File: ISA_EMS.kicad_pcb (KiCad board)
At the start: 2 copper layers, 176.5 x 85.1 mm, 49 parts, among them J1 ISA BUS, J2 EMS Address, U10 74HCT32, U11 74HCT04, U12 74LS245, U13 AS6C4008-55PCN, U14 AS6C4008-55PCN, U15 AS6C4008-55PCN, U16 AS6C4008-55PCN, U17 74HCT138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

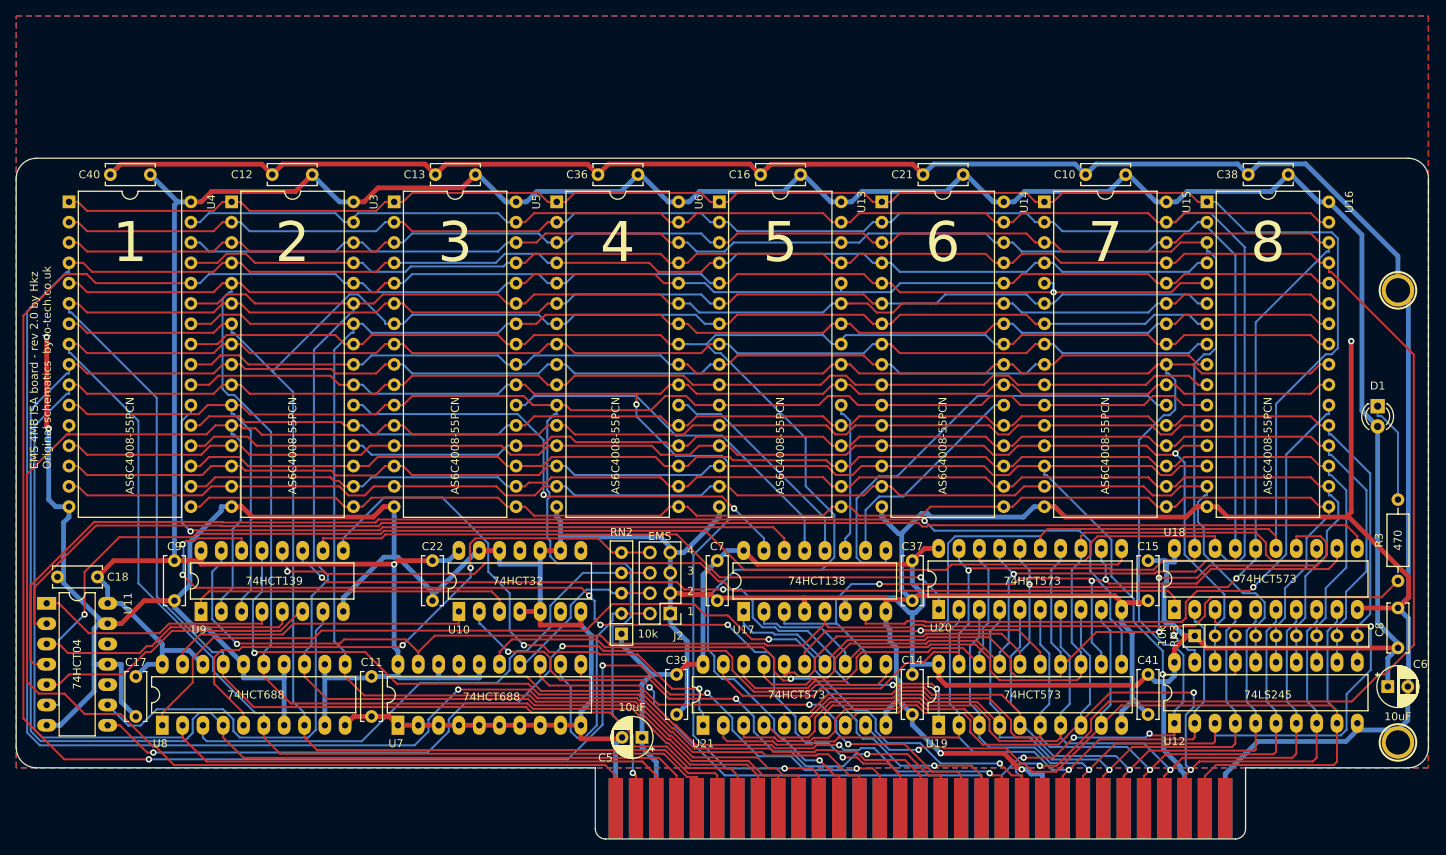
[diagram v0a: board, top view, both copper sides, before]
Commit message: Replace components on board
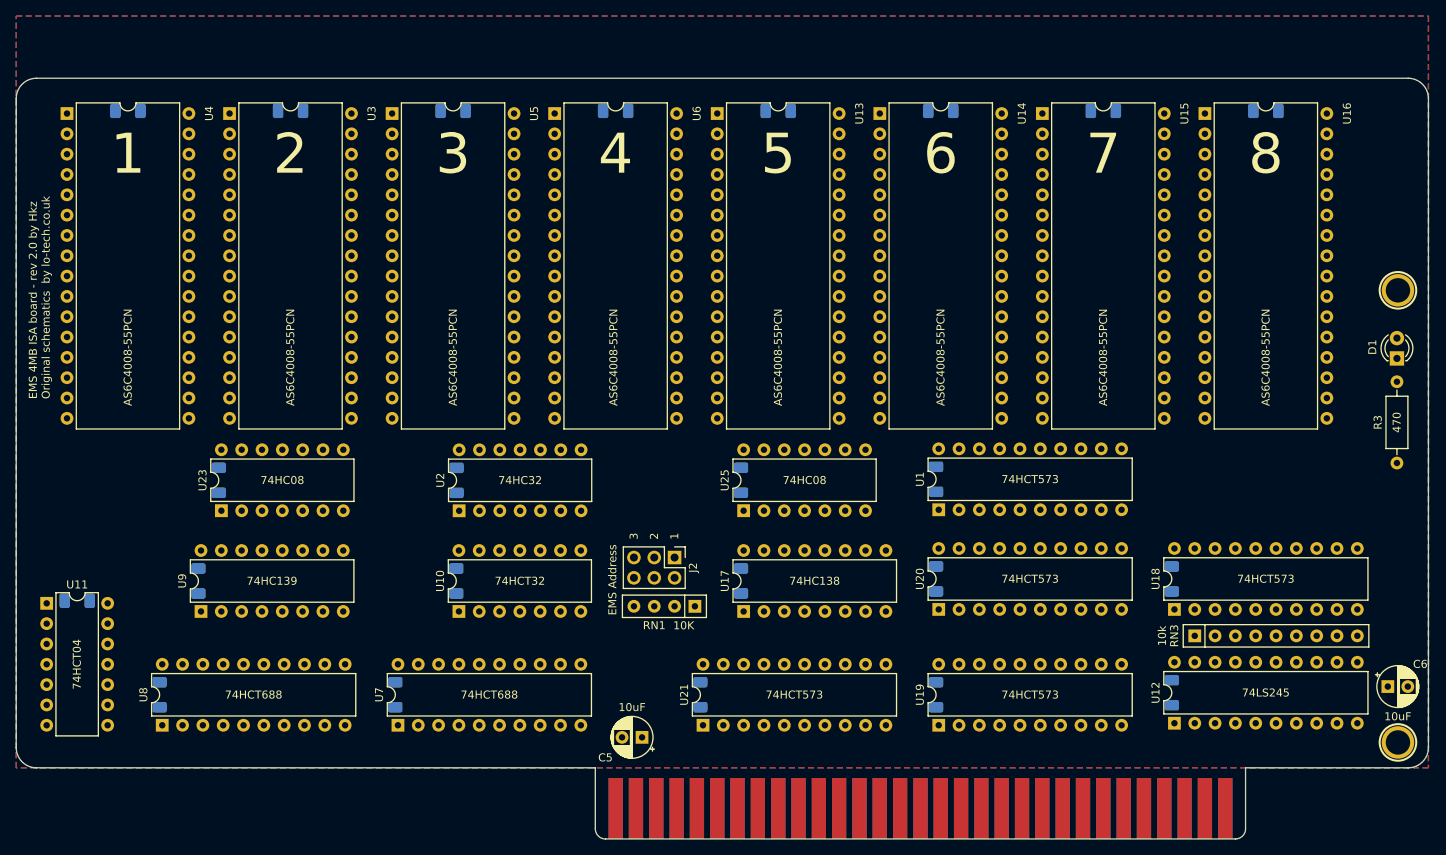
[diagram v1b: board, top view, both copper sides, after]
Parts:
- removed RN2: 10k, Resistor_THT:R_Array_SIP5
- added C1: 100nF, Capacitor_SMD:C_1206_3216Metric_Pad1.33x1.80mm_HandSolder, B.Cu at (193.5, 158.4)
- added C2: 100nF, Capacitor_SMD:C_1206_3216Metric_Pad1.33x1.80mm_HandSolder, B.Cu at (163.7, 158.4)
- added C3: 100nF, Capacitor_SMD:C_1206_3216Metric_Pad1.33x1.80mm_HandSolder, B.Cu at (253.4, 158.2)
- added RN1: 10K, Resistor_THT:R_Array_SIP4, F.Cu at (223.3, 174.1)
- added U1: 74HCT573, Package_DIP:DIP-20_W7.62mm, F.Cu at (253.7, 162.1)
- added U2: 74HC32, Package_DIP:DIP-14_W7.62mm, F.Cu at (193.8, 162.2)
- added U23: 74HC08, Package_DIP:DIP-14_W7.62mm, F.Cu at (164.1, 162.2)
- added U25: 74HC08, Package_DIP:DIP-14_W7.62mm, F.Cu at (229.4, 162.2)
- C10, C11, C12, C13, C14, C15, C16, C17, C18, C21, C22, C36, C37, C38, C39, C40, C41, C7, C8, C9: footprint Capacitor_THT:C_Disc_D6.0mm_W2.5mm_P5.00mm -> Capacitor_SMD:C_1206_3216Metric_Pad1.33x1.80mm_HandSolder; moved to B.Cu
- J2: footprint Connector_PinHeader_2.54mm:PinHeader_2x04_P2.54mm_Vertical -> Connector_PinHeader_2.54mm:PinHeader_2x03_P2.54mm_Vertical
- U10, U11: footprint Package_DIP:DIP-14_W7.62mm_LongPads -> Package_DIP:DIP-14_W7.62mm
- U12, U18, U19, U20, U21, U7, U8: footprint Package_DIP:DIP-20_W7.62mm_LongPads -> Package_DIP:DIP-20_W7.62mm
- U17: value 74HCT138 -> 74HC138; footprint Package_DIP:DIP-16_W7.62mm_LongPads -> Package_DIP:DIP-16_W7.62mm
- U9: value 74HCT139 -> 74HC139; footprint Package_DIP:DIP-16_W7.62mm_LongPads -> Package_DIP:DIP-16_W7.62mm
- moved C8 84.8 mm to (229.0, 158.4), turned to -90 degrees
- moved R3 14.7 mm to (311.0, 156.2)
- moved U13 11.0 mm to (226.1, 112.5)
- moved U14 11.0 mm to (246.4, 112.5)
- moved U15 11.0 mm to (266.7, 112.5)
- moved U16 11.0 mm to (287.0, 112.5)
- moved U3 11.0 mm to (165.1, 112.5)
- moved U4 11.0 mm to (144.8, 112.5)
- moved U5 11.0 mm to (185.4, 112.5)
- moved U6 11.0 mm to (205.7, 112.5)
- moved C38 8.44 mm to (294.6, 112.2)
- moved C13 8.44 mm to (193.0, 112.2)
- moved C10 8.44 mm to (274.3, 112.2)
- moved C16 8.44 mm to (233.7, 112.2)
- moved C21 8.44 mm to (254.0, 112.2)
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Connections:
- net /~IOW renamed /~{IOW}
- net /~MEMR renamed /~{MEMR}
- net /~MEMW renamed /~{MEMW}
- net /~RAM-CS0 renamed /~{RAM-CS0}
- net /~RAM-CS1 renamed /~{RAM-CS1}
- net /~RAM-CS2 renamed /~{RAM-CS2}
- net /~RAM-CS3 renamed /~{RAM-CS3}
- net /~RAM-CS4 renamed /~{RAM-CS4}
- net /~RAM-CS5 renamed /~{RAM-CS5}
- net /~RAM-CS6 renamed /~{RAM-CS6}
- net /~RAM-CS7 renamed /~{RAM-CS7}
- net /~RAM-SELECT renamed /~{RAM-SELECT}
- net /~REG0-OE renamed /~{REG0-OE}
- net /~REG1-OE renamed /~{REG1-OE}
- net /~REG2-OE renamed /~{REG2-OE}
- net /~REG3-OE renamed /~{REG3-OE}
- J1 pad 14: (no net) -> /~{IOR}
- J1 pad 15: (no net) -> unconnected-(J1-~{DACK3}-Pad15)
- J1 pad 16: (no net) -> unconnected-(J1-DRQ3-Pad16)
- J1 pad 17: (no net) -> unconnected-(J1-~{DACK1}-Pad17)
- J1 pad 18: (no net) -> unconnected-(J1-DRQ1-Pad18)
- J1 pad 19: (no net) -> unconnected-(J1-~{DACK0}-Pad19)
- J1 pad 2: (no net) -> /RESETDRV
- J1 pad 20: (no net) -> unconnected-(J1-CLK-Pad20)
- J1 pad 21: (no net) -> /IRQ7
- J1 pad 22: (no net) -> /IRQ6
- J1 pad 23: (no net) -> /IRQ5
- J1 pad 24: (no net) -> /IRQ4
- J1 pad 25: (no net) -> /IRQ3
- J1 pad 26: (no net) -> /~{DACK2}
- J1 pad 27: (no net) -> /TC
- J1 pad 28: (no net) -> unconnected-(J1-ALE-Pad28)
- J1 pad 30: (no net) -> unconnected-(J1-OSC-Pad30)
- J1 pad 32: (no net) -> unconnected-(J1-IO-Pad32)
- J1 pad 4: (no net) -> unconnected-(J1-IRQ2-Pad4)
- J1 pad 41: (no net) -> unconnected-(J1-IO_READY-Pad41)
- J1 pad 5: (no net) -> unconnected-(J1--5V-Pad5)
- J1 pad 6: (no net) -> /DRQ2
- J1 pad 7: (no net) -> -12V
- J1 pad 8: (no net) -> unconnected-(J1-UNUSED-Pad8)
- J1 pad 9: (no net) -> +12V
- U10 pad 10: GND -> Net-(U10-Pad10)
- U10 pad 11: (no net) -> unconnected-(U10-Pad11)
- U10 pad 4: GND -> Net-(U10-Pad3)
- U10 pad 5: GND -> /A2
- U10 pad 6: (no net) -> Net-(U9A-E)
- U10 pad 8: (no net) -> Net-(U10-Pad8)
- U10 pad 9: GND -> Net-(U10-Pad3)
- U11 pad 10: (no net) -> Net-(U10-Pad10)
- U11 pad 11: GND -> /A2
- U11 pad 12: (no net) -> Net-(U1-Load)
- U11 pad 13: GND -> Net-(U10-Pad8)
- U17 pad 4: GND -> /RAM-DISABLED
- U8 pad 2: /A2 -> GND
- U8 pad 3: /JP3 -> GND
- U8 pad 5: /JP4 -> /JP3
- U9 pad 1: Net-(U10-Pad3) -> Net-(U9A-E)
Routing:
- net GND: track 825.8 -> 0.00 mm, vias 5 -> 0
- net VCC: track 600.8 -> 0.00 mm, vias 1 -> 0
- net /A13: track 352.3 -> 0.00 mm, vias 4 -> 0
- net /A12: track 327.0 -> 0.00 mm, vias 1 -> 0
- net /RAM-A18: track 304.4 -> 0.00 mm, vias 1 -> 0
- net /A0: track 290.2 -> 0.00 mm
- net /RAM-A15: track 290.0 -> 0.00 mm
- net /A3: track 288.7 -> 0.00 mm
- net /A2: track 281.1 -> 0.00 mm
- net /A6: track 278.6 -> 0.00 mm
- net /RAM-A17: track 274.7 -> 0.00 mm, vias 2 -> 0
- net /A7: track 274.2 -> 0.00 mm, vias 1 -> 0
- net /RAM-A16: track 273.0 -> 0.00 mm, vias 1 -> 0
- net /RAM-A14: track 270.9 -> 0.00 mm, vias 1 -> 0
- net /A4: track 268.9 -> 0.00 mm
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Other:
- board size 176.5 x 85.1 mm -> 176.5 x 95.1 mm
- net class Default removed
- net class POWER removed
- net class POWR_SMALL removed
- board text added: "260-267h"
- board text added: "268-26Fh"
- board text removed: "260-263h"
- board text removed: "264-267h"
- board text removed: "268-26Bh"
- board text removed: "26C-26Fh"
- board text removed: "EMS"

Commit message: Begin routing
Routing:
- net /D7: track 0.00 -> 97.6 mm, vias 0 -> 2
- net /D6: track 0.00 -> 96.2 mm, vias 0 -> 2
- net VCC: track 0.00 -> 95.9 mm
- net /D5: track 0.00 -> 95.6 mm, vias 0 -> 2
- net /D4: track 0.00 -> 94.5 mm, vias 0 -> 2
- net /D3: track 0.00 -> 93.3 mm, vias 0 -> 2
- net /D2: track 0.00 -> 92.3 mm, vias 0 -> 2
- net /D1: track 0.00 -> 90.8 mm, vias 0 -> 2
- net /D0: track 0.00 -> 88.3 mm
- net GND: track 0.00 -> 22.9 mm
- net /JP3: track 0.00 -> 3.56 mm
- net /JP2: track 0.00 -> 3.56 mm
- net /JP1: track 0.00 -> 3.56 mm
- net /DB7: track 0.00 -> 3.30 mm
- net /DB6: track 0.00 -> 3.30 mm
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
